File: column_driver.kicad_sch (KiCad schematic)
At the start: 24 parts, among them U10 LED1642GW, U3 LED1642GW, U4 LED1642GW, U5 LED1642GW, U6 LED1642GW, U7 LED1642GW, U8 LED1642GW, U9 LED1642GW

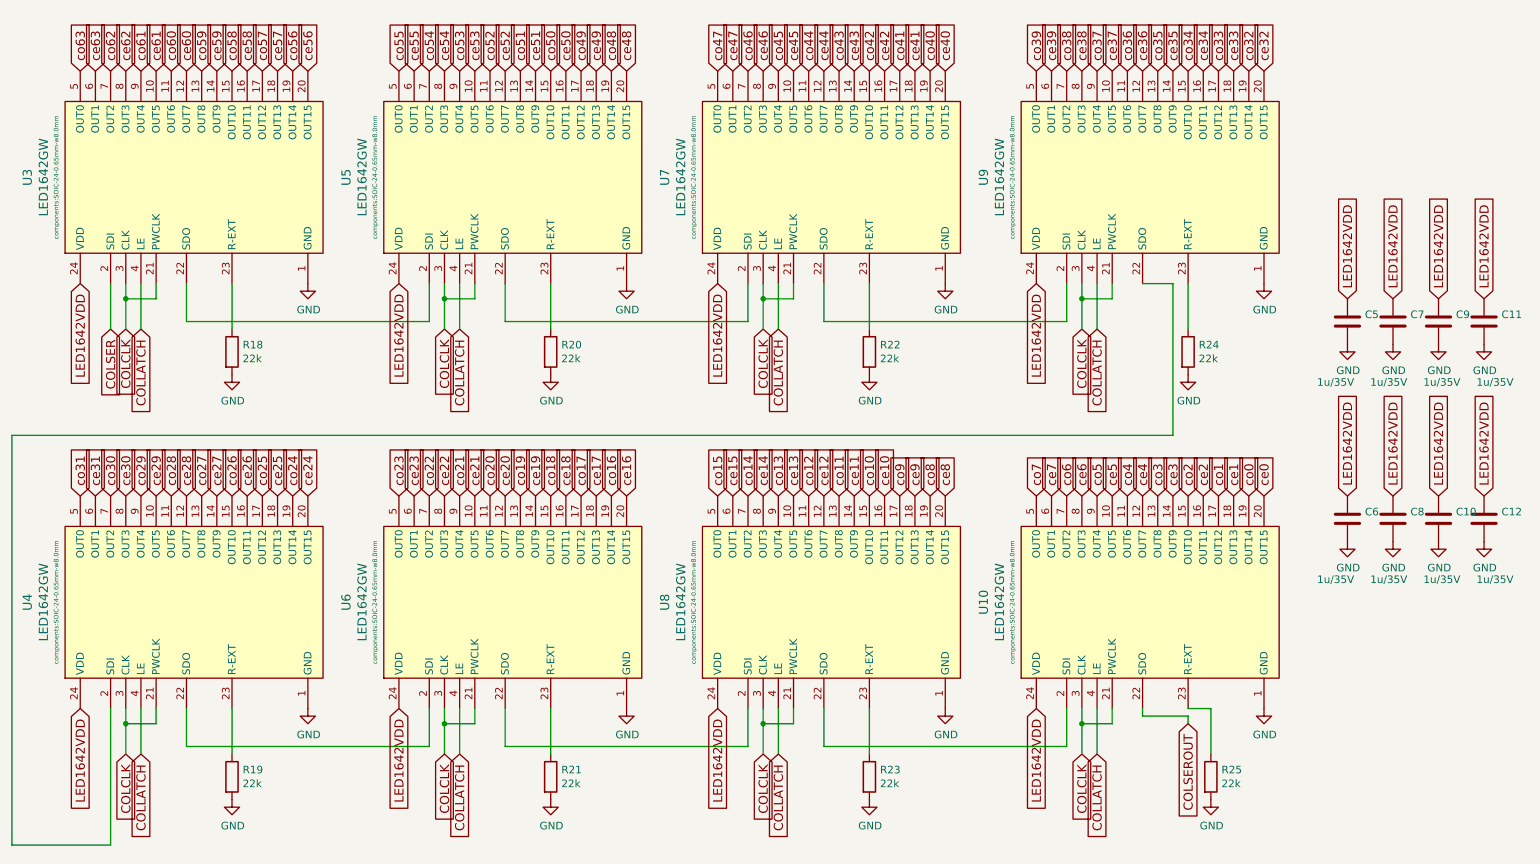
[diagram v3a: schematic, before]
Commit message: WROOM32 coupling capacitor order fixed; Added FB on long line to board left-most sensors
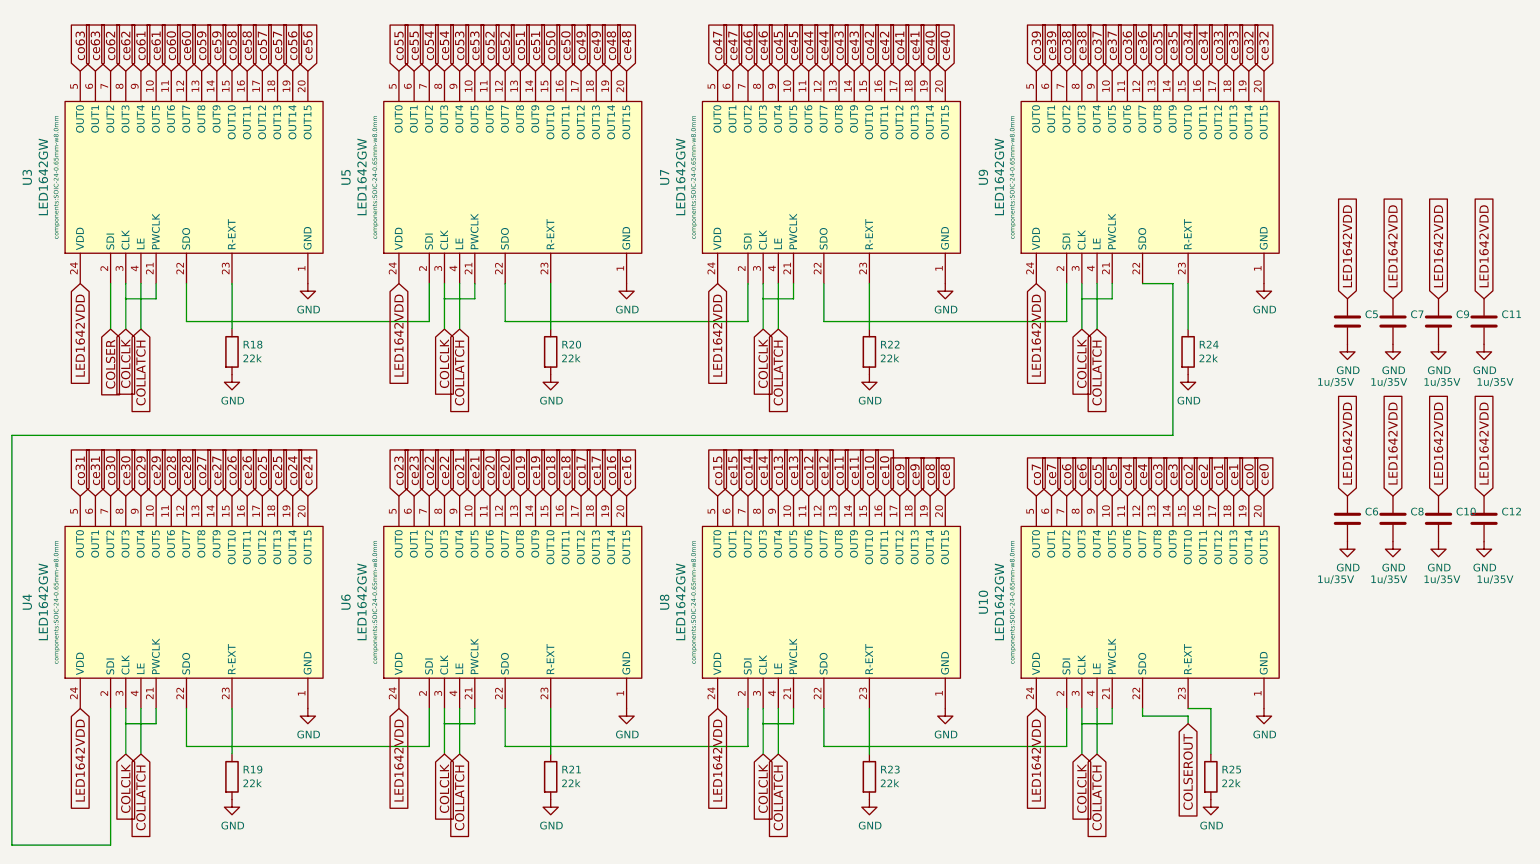
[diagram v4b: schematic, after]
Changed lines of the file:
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@@
-(kicad_sch (version 20200618) (host eeschema "5.99.0-unknown-7340c97~89~ubuntu18.04.1")
-  (page 1 10)
+(kicad_sch (version 20200714) (host eeschema "5.99.0-unknown-e5f2015a9~89~ubuntu18.04.1")
+  (page 8 10)
   (paper "A4")
-  (junction (at 34.29 62.23) (diameter 0) (color 0 0 0 0))
-  (junction (at 34.29 133.35) (diameter 0) (color 0 0 0 0))
-  (junction (at 87.63 62.23) (diameter 0) (color 0 0 0 0))
-  (junction (at 87.63 133.35) (diameter 0) (color 0 0 0 0))
-  (junction (at 140.97 62.23) (diameter 0) (color 0 0 0 0))
-  (junction (at 140.97 133.35) (diameter 0) (color 0 0 0 0))
-  (junction (at 194.31 62.23) (diameter 0) (color 0 0 0 0))
-  (junction (at 194.31 133.35) (diameter 0) (color 0 0 0 0))
+  (junction (at 34.29 62.23) (diameter 0.3048) (color 0 0 0 0))
+  (junction (at 34.29 133.35) (diameter 0.3048) (color 0 0 0 0))
+  (junction (at 87.63 62.23) (diameter 0.3048) (color 0 0 0 0))
+  (junction (at 87.63 133.35) (diameter 0.3048) (color 0 0 0 0))
+  (junction (at 140.97 62.23) (diameter 0.3048) (color 0 0 0 0))
+  (junction (at 140.97 133.35) (diameter 0.3048) (color 0 0 0 0))
+  (junction (at 194.31 62.23) (diameter 0.3048) (color 0 0 0 0))
+  (junction (at 194.31 133.35) (diameter 0.3048) (color 0 0 0 0))
   (wire (pts (xy 15.24 85.09) (xy 15.24 153.67))
     (stroke (width 0) (type solid) (color 0 0 0 0))
